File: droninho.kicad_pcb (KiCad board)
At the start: 2 copper layers, 49 x 72.2 mm, 34 parts, among them J6 I2C, J7 TXD0/RXD0, J8 I2C, Q1 Si2300DS, Q2 Si2300DS, Q3 Si2300DS, Q4 Si2300DS, SW1 KMR241G LFS, U1 AMS1117-3.3, U2 MPU9250/6500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

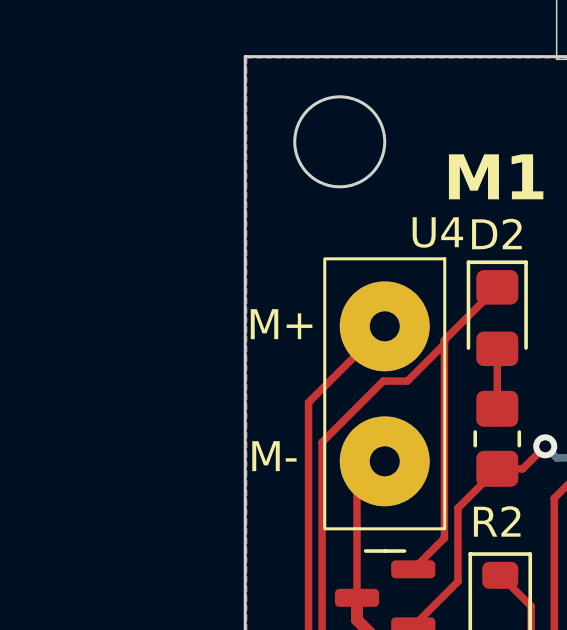
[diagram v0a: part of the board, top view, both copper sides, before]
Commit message: add manufacturer and part number for BOM.
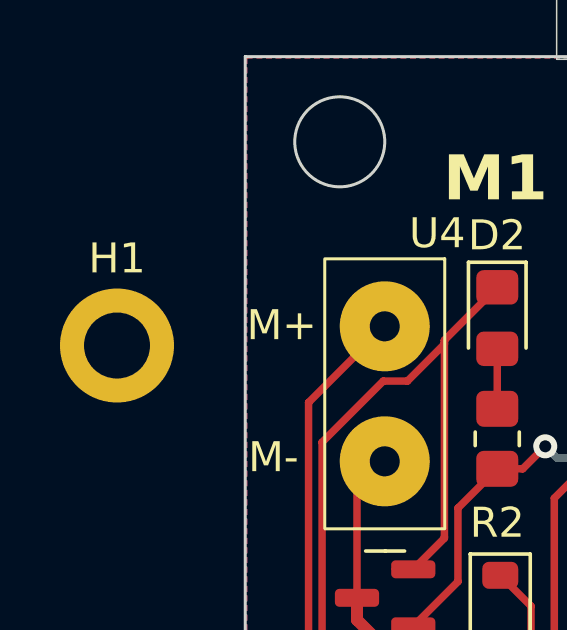
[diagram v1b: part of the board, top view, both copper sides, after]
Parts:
- added H1: MountingHole_Pad_MP, MountingHole:MountingHole_2.2mm_M2_DIN965_Pad, F.Cu at (116.8, 75.7)
- C3: value 0.1uF/50V(10%) -> 0.1uF/10V(5%)
- R1, R2, R3, R4, R5: value 10K(5%) -> 10K(1%)

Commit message: BOM updated.
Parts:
- removed H1: MountingHole_Pad_MP, MountingHole:MountingHole_2.2mm_M2_DIN965_Pad
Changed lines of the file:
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@@
 		)
 	)
-	(footprint "MountingHole:MountingHole_2.2mm_M2_DIN965_Pad"
-		(layer "F.Cu")
-		(at 116.775 75.69)
-		(descr "Mounting Hole 2.2mm, M2, DIN965")
-		(tags "mounting hole 2.2mm m2 din965")
-		(property "Reference" "H1"
-			(at 0 -2.9 0)
-			(layer "F.SilkS")
-			(effects
-				(font
-					(size 1 1)
-					(thickness 0.15)
-				)
-			)
-		)
-		(property "Value" "MountingHole_Pad_MP"
-			(at 0 2.9 0)
-			(layer "F.Fab")
-			(effects
-				(font
-					(size 1 1)
-					(thickness 0.15)
-				)
-			)
-		)
-		(property "Datasheet" ""
-			(at 0 0 0)
-			(unlocked yes)
-			(layer "F.Fab")
-			(hide yes)
-			(effects
-				(font
-					(size 1.27 1.27)
-					(thickness 0.15)
-				)
-			)
-		)
-		(property "Description" "Mounting Hole with connection as pad named MP"
-			(at 0 0 0)
-			(unlocked yes)
-			(layer "F.Fab")
-			(hide yes)
-			(effects
-				(font
-					(size 1.27 1.27)
-					(thickness 0.15)
-				)
-			)
-		)
-		(property "Manufacturer" ""
-			(at 0 0 0)
-			(unlocked yes)
-			(layer "F.Fab")
-			(hide yes)
-			(effects
-				(font
-					(size 1 1)
-					(thickness 0.15)
-				)
-			)
-		)
-		(property "Mfg Part #" ""
-			(at 0 0 0)
-			(unlocked yes)
-			(layer "F.Fab")
-			(hide yes)
-			(effects
-				(font
-					(size 1 1)
-					(thickness 0.15)
-				)
-			)
-		)
-		(property "Package/Footprint" ""
-			(at 0 0 0)
-			(unlocked yes)
-			(layer "F.Fab")
-			(hide yes)
-			(effects
-				(font
-					(size 1 1)
-					(thickness 0.15)
-				)
-			)
-		)
-		(property "Type" ""
-			(at 0 0 0)
-			(unlocked yes)
-			(layer "F.Fab")
-			(hide yes)
-			(effects
-				(font
-					(size 1 1)
-					(thickness 0.15)
-				)
-			)
-		)
-		(property "Designator" ""
-			(at 0 0 0)
-			(unlocked yes)
-			(layer "F.Fab")
-			(hide yes)
-			(effects
-				(font
-					(size 1 1)
-					(thickness 0.15)
-				)
-			)
-		)
-		(property ki_fp_filters "MountingHole*Pad*")
-		(sheetname "/")
-		(sheetfile "droninho.kicad_sch")
-		(attr exclude_from_pos_files exclude_from_bom)
-		(fp_circle
-			(center 0 0)
-			(end 1.9 0)
-			(stroke
-				(width 0.15)
-				(type solid)
-			)
-			(fill no)
-			(layer "Cmts.User")
-		)
-		(fp_circle
-			(center 0 0)
-			(end 2.15 0)
-			(stroke
-				(width 0.05)
-				(type solid)
-			)
-			(fill no)
-			(layer "F.CrtYd")
-		)
-		(fp_text user "${REFERENCE}"
-			(at 0 0 0)
-			(layer "F.Fab")
-			(effects
-				(font
-					(size 1 1)
-					(thickness 0.15)
-				)
-			)
-		)
-		(pad "1" thru_hole circle
-			(at 0 0)
-			(size 3.8 3.8)
-			(drill 2.2)
-			(layers "*.Cu" "*.Mask")
-			(remove_unused_layers no)
-		)
-		(embedded_fonts no)
-	)
 	(footprint "Package_TO_SOT_SMD:SOT-23"
 		(layer "F.Cu")
@@
 			)
 		)
+		(property "Manufacturer" "Molex"
+			(at 0 0 180)
+			(unlocked yes)
+			(layer "F.Fab")
+			(hide yes)
+			(effects
+				(font
+					(size 1 1)
+					(thickness 0.15)
+				)
+			)
+		)
+		(property "Mfg Part #" "502603-0470"
+			(at 0 0 180)
+			(unlocked yes)
+			(layer "F.Fab")
+			(hide yes)
+			(effects
+				(font
+					(size 1 1)
+					(thickness 0.15)
+				)
+			)
+		)
+		(property "Package/Footprint" "4POS"
+			(at 0 0 180)
+			(unlocked yes)
+			(layer "F.Fab")
+			(hide yes)
+			(effects
+				(font
+					(size 1 1)
+					(thickness 0.15)
+				)
+			)
+		)
+		(property "Type" "THT"
+			(at 0 0 180)
+			(unlocked yes)
+			(layer "F.Fab")
+			(hide yes)
+			(effects
+				(font
+					(size 1 1)
+					(thickness 0.15)
+				)
+			)
+		)
+		(property "Designator" "J7"
+			(at 0 0 180)
+			(unlocked yes)
+			(layer "F.Fab")
+			(hide yes)
+			(effects
+				(font
+					(size 1 1)
+					(thickness 0.15)
+				)
+			)
+		)
 		(property ki_fp_filters "Connector*:*_1x??_*")
 		(sheetname "/")
@@
 			)
 		)
+		(property "Manufacturer" "Molex"
+			(at 0 0 180)
+			(unlocked yes)
+			(layer "F.Fab")
+			(hide yes)
+			(effects
+				(font
+					(size 1 1)
+					(thickness 0.15)
+				)
+			)
+		)
+		(property "Mfg Part #" "502603-0470"
+			(at 0 0 180)
+			(unlocked yes)
+			(layer "F.Fab")
+			(hide yes)
+			(effects
+				(font
+					(size 1 1)
+					(thickness 0.15)
+				)
+			)
+		)
+		(property "Package/Footprint" "4POS"
+			(at 0 0 180)
+			(unlocked yes)
+			(layer "F.Fab")
+			(hide yes)
+			(effects
+				(font
+					(size 1 1)
+					(thickness 0.15)
+				)
+			)
+		)
+		(property "Type" "THT"
+			(at 0 0 180)
+			(unlocked yes)
+			(layer "F.Fab")
+			(hide yes)
+			(effects
+				(font
+					(size 1 1)
+					(thickness 0.15)
+				)
+			)
+		)
+		(property "Designator" "J8"
+			(at 0 0 180)
+			(unlocked yes)
+			(layer "F.Fab")
+			(hide yes)
+			(effects
+				(font
+					(size 1 1)
+					(thickness 0.15)
+				)
+			)
+		)
 		(property ki_fp_filters "Connector*:*_1x??_*")
 		(sheetname "/")
@@
 			)
 		)
+		(property "Manufacturer" "C&K"
+			(at 0 0 0)
+			(unlocked yes)
+			(layer "F.Fab")
+			(hide yes)
+			(effects
+				(font
+					(size 1 1)
+					(thickness 0.15)
+				)
+			)
+		)
+		(property "Mfg Part #" "KMR241G LFS"
+			(at 0 0 0)
+			(unlocked yes)
+			(layer "F.Fab")
+			(hide yes)
+			(effects
+				(font
+					(size 1 1)
+					(thickness 0.15)
+				)
+			)
+		)
+		(property "Package/Footprint" "SW_Push_1P1T_NO_CK_KMR2"
+			(at 0 0 0)
+			(unlocked yes)
+			(layer "F.Fab")
+			(hide yes)
+			(effects
+				(font
+					(size 1 1)
+					(thickness 0.15)
+				)
+			)
+		)
+		(property "Type" "SMT"
+			(at 0 0 0)
+			(unlocked yes)
+			(layer "F.Fab")
+			(hide yes)
+			(effects
+				(font
+					(size 1 1)
+					(thickness 0.15)
+				)
+			)
+		)
+		(property "Designator" "SW1"
+			(at 0 0 0)
+			(unlocked yes)
+			(layer "F.Fab")
+			(hide yes)
+			(effects
+				(font
+					(size 1 1)
+					(thickness 0.15)
+				)
+			)
+		)
 		(sheetname "/")
 		(sheetfile "droninho.kicad_sch")
@@
 			(at 0 0 0)
 			(unlocked yes)
+			(layer "F.Fab")
+			(hide yes)
+			(effects
+				(font
+					(size 1 1)
+					(thickness 0.15)
+				)
+			)
+		)
+		(property "Manufacturer" "Molex"
+			(at 0 0 0)
+			(unlocked yes)
+			(layer "F.Fab")
+			(hide yes)
+			(effects
+				(font
+					(size 1 1)
+					(thickness 0.15)
+				)
+			)
+		)
+		(property "Mfg Part #" "502603-0470"
+			(at 0 0 0)
+			(unlocked yes)
+			(layer "F.Fab")
+			(hide yes)
+			(effects
+				(font
+					(size 1 1)
+					(thickness 0.15)
+				)
+			)
+		)
+		(property "Package/Footprint" "4POS"
+			(at 0 0 0)
+			(unlocked yes)
+			(layer "F.Fab")
+			(hide yes)
+			(effects
+				(font
+					(size 1 1)
+					(thickness 0.15)
+				)
+			)
+		)
+		(property "Type" "THT"
+			(at 0 0 0)
+			(unlocked yes)
+			(layer "F.Fab")
+			(hide yes)
+			(effects
+				(font
+					(size 1 1)
+					(thickness 0.15)
+				)
+			)
+		)
+		(property "Designator" "J6"
+			(at 0 0 0)
+			(unlocked yes)

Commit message: first commit
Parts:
- added C4: 0.1uF/10V(5%), Capacitor_SMD:C_0402_1005Metric, F.Cu at (146.0, 125.2)
- added C5: 0.1uF/10V(5%), Capacitor_SMD:C_0402_1005Metric, F.Cu at (148.9, 121.1)
- added C6: 0.1uF/10V(5%), Capacitor_SMD:C_0402_1005Metric, F.Cu at (155.9, 126.2)
- added C7: 0.1uF/10V(5%), Capacitor_SMD:C_0402_1005Metric, F.Cu at (155.9, 128.2)
- added C8: C_Small_US, Capacitor_SMD:C_0201_0603Metric, F.Cu at (155.7, 130.0)
- added U8: ICM-20948, Sensor_Motion:InvenSense_QFN-24_3x3mm_P0.4mm, F.Cu at (144.9, 121.6)
- U2: value MPU9250/6500 -> TLV70218_SOT23-5; footprint Library:MPU-9250-6500 -> Package_TO_SOT_SMD:SOT-23-5
- moved U2 19.6 mm to (151.9, 127.6), turned to 0 degrees
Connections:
- U2 pad 1: /+3.3V -> Net-(U2-EN)
- U2 pad 3: /SCL -> Net-(U2-EN)
- U2 pad 4: /SDA -> unconnected-(U2-NC-Pad4)
- U2 pad 5: unconnected-(U2-EDA-Pad5) -> Net-(U2-OUT)
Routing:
- net GND: track 228.1 -> 0.00 mm, vias 3 -> 0
- net /+3.3V: track 199.1 -> 0.00 mm, vias 5 -> 0
- net /PWM3: track 80.6 -> 0.00 mm, vias 2 -> 0
- net /PWM4: track 77.0 -> 0.00 mm, vias 3 -> 0
- net /SCL: track 72.0 -> 0.00 mm, vias 1 -> 0
- net /SDA: track 65.9 -> 0.00 mm, vias 1 -> 0
- net /PWM2: track 59.4 -> 0.00 mm, vias 2 -> 0
- net /TXD0: track 54.0 -> 0.00 mm, vias 1 -> 0
- net /TXD2: track 48.5 -> 0.00 mm, vias 2 -> 0
- net /BAT+: track 48.3 -> 0.00 mm, vias 4 -> 0
- net /RXD0: track 47.6 -> 0.00 mm, vias 1 -> 0
- net /RXD2: track 42.2 -> 0.00 mm, vias 2 -> 0
- net /PWM1: track 36.4 -> 0.00 mm, vias 1 -> 0
- net /Push_button: track 31.8 -> 0.00 mm
- net /M4-: track 11.4 -> 0.00 mm, vias 1 -> 0
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- removed copper zone on B.Cu, net GND
- removed copper zone on F.Cu, net GND
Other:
- outline, holes or cut-outs redrawn
- board text removed: "MPU925/6500"

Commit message: driver PCB ready
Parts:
- removed C3: 0.1uF/10V(5%), Capacitor_SMD:C_0805_2012Metric_Pad1.18x1.45mm_HandSolder
- removed C4, C5, C6, C7: 0.1uF/10V(5%), Capacitor_SMD:C_0402_1005Metric
- removed C8: C_Small_US, Capacitor_SMD:C_0201_0603Metric
- removed J6, J8: I2C, Connector_PinHeader_2.54mm:PinHeader_1x04_P2.54mm_Vertical
- removed J7: TXD0/RXD0, Connector_PinHeader_2.54mm:PinHeader_1x04_P2.54mm_Vertical
- removed SW1: KMR241G LFS, Button_Switch_SMD:SW_Push_1P1T_NO_CK_KMR2
- removed U2: TLV70218_SOT23-5, Package_TO_SOT_SMD:SOT-23-5
- removed U3: ESP32 ESP-WROOM-32 DEVKit V1, Library:ESP32_30pin vertical WIFI
- removed U4, U5, U6, U7: Through Hole Connector, Library:Connector_Motor
- removed U8: ICM-20948, Sensor_Motion:InvenSense_QFN-24_3x3mm_P0.4mm
- added J1: Conn_01x06_Socket, Connector_Hirose:Hirose_DF13-06P-1.25DSA_1x06_P1.25mm_Vertical, F.Cu at (61.9, 57.5)
- added J2: Conn_01x02_Socket, Connector_Hirose:Hirose_DF13-02P-1.25DSA_1x02_P1.25mm_Vertical, F.Cu at (54.6, 58.5)
- added J3: Conn_01x02_Socket, Connector_Hirose:Hirose_DF13-02P-1.25DSA_1x02_P1.25mm_Vertical, F.Cu at (75.6, 57.4)
- added J4: Conn_01x02_Socket, Connector_Hirose:Hirose_DF13-02P-1.25DSA_1x02_P1.25mm_Vertical, F.Cu at (75.7, 71.8)
- added J5: Conn_01x02_Socket, Connector_Hirose:Hirose_DF13-02P-1.25DSA_1x02_P1.25mm_Vertical, F.Cu at (54.4, 72.9)
- moved R3 112.9 mm to (70.3, 61.5)
- moved D3 108.6 mm to (72.6, 61.5), turned to 90 degrees
- moved R5 103.3 mm to (58.2, 69.2), turned to 180 degrees
- moved Q3 101.9 mm to (76.5, 67.9)
- moved D5 100.6 mm to (60.6, 71.3), turned to 180 degrees
- moved H4 100.4 mm to (68.1, 75.0)
- moved H3 100.4 mm to (62.3, 75.0)
- moved D8 98.9 mm to (72.8, 73.7)
- moved D7 93.2 mm to (72.5, 57.0)
- moved C1 92.2 mm to (59.3, 66.5)
- moved Q2 91.7 mm to (76.5, 62.6)
- moved Q4 90.0 mm to (53.3, 67.8)
- moved D9 85.8 mm to (57.4, 74.0)
- moved R4 83.8 mm to (72.0, 69.2), turned to 180 degrees
- moved D4 81.1 mm to (69.7, 71.4), turned to 0 degrees
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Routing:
- net GND: track 0.00 -> 86.0 mm, vias 0 -> 7
- net /+3.3V: track 0.00 -> 76.0 mm, vias 0 -> 5
- net /BAT+: track 0.00 -> 25.3 mm, vias 0 -> 2
- net /PWM4: track 0.00 -> 23.9 mm, vias 0 -> 1
- net /PWM3: track 0.00 -> 20.6 mm, vias 0 -> 2
- net /PWM2: track 0.00 -> 18.9 mm, vias 0 -> 2
- net /PWM1: track 0.00 -> 13.5 mm
- net /M4-: track 0.00 -> 10.3 mm
- net /M2-: track 0.00 -> 10.3 mm
- net /M1-: track 0.00 -> 8.16 mm
- net /M3-: track 0.00 -> 7.57 mm
- net Net-(D5-A): track 0.00 -> 3.26 mm
- net Net-(D4-A): track 0.00 -> 2.34 mm
- net Net-(D3-A): track 0.00 -> 2.32 mm
- net Net-(D2-A): track 0.00 -> 2.21 mm
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- added copper zone on B.Cu, net GND
- added copper zone on F.Cu, net GND
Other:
- board size 49 x 72.2 mm -> 30 x 30 mm
- board text added: "+ -"
- board text added: "+3.3v"
- board text added: "- +"
- board text added: "12v max"
- board text added: "B+"
- board text added: "B-"
- board text added: "PWM1"
- board text added: "PWM2"
- board text added: "PWM3"
- board text added: "PWM4"
- board text added: "UFABC"
- board text added: "V1.1"
- board text added: "github.com/dferruzzo/Droninho/tree/driver"
- board text removed: "3.3v"
- board text removed: "BAT+"
- board text removed: "BAT-"
- board text removed: "Droninho Taphros 2025 v1.0"
- board text removed: "ESP32-DevKit"
- board text removed: "RX0"
- board text removed: "RX2"
- board text removed: "SCL"
- board text removed: "SDA"
- board text removed: "TX0"
- board text removed: "TX2"
- board text removed: "https://github.com/dferruzzo/Droninho"

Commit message: small updates
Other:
- board text added: "M1+ M1-"
- board text added: "M2- M2+"
- board text added: "M3- M3+"
- board text added: "M4+ M4-"
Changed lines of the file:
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@@
+		)
+	)
+	(gr_text "12v\nmax"
+		(at 65 79.5 0)
+		(layer "F.SilkS")
+		(effects
+			(font
+				(size 1 1)
+				(thickness 0.15)
+			)
+			(justify bottom)
 		)
 	)
 	(gr_text "PWM4"
-		(at 68.8 54.8 90)
+		(at 68.85 54.8 90)
 		(layer "F.SilkS")
 		(effects
@@
 	)
 	(gr_text "+3.3v"
-		(at 62.3 54.8 90)
+		(at 62.25 54.8 90)
 		(layer "F.SilkS")
 		(effects
@@
 		)
 	)
-	(gr_text "12v\nmax"
-		(at 63.6 79.7 0)
-		(layer "F.SilkS")
-		(effects
-			(font
-				(size 1 1)
-				(thickness 0.15)
-			)
-			(justify left bottom)
-		)
-	)
 	(gr_text "+\n-"
 		(at 50.1 73.9 0)
@@
 		)
 	)
+	(gr_text "PWM1"
+		(at 64.9 53.3 90)
+		(layer "B.SilkS")
+		(effects
+			(font
+				(size 0.8 0.75)
+				(thickness 0.15)
+			)
+			(justify left bottom mirror)
+		)
+	)
+	(gr_text "M3-\nM3+"
+		(at 79.8 73.85 0)
+		(layer "B.SilkS")
+		(effects
+			(font
+				(size 1 1)
+				(thickness 0.15)
+			)
+			(justify left bottom mirror)
+		)
+	)
+	(gr_text "PWM3"
+		(at 67.5 53.3 90)
+		(layer "B.SilkS")
+		(effects
+			(font
+				(size 0.8 0.75)
+				(thickness 0.15)
+			)
+			(justify left bottom mirror)
+		)
+	)
+	(gr_text "PWM4"
+		(at 68.8 53.3 90)
+		(layer "B.SilkS")
+		(effects
+			(font
+				(size 0.8 0.75)
+				(thickness 0.15)
+			)
+			(justify left bottom mirror)
+		)
+	)
+	(gr_text "M2-\nM2+"
+		(at 79.7 59.45 0)
+		(layer "B.SilkS")
+		(effects
+			(font
+				(size 1 1)
+				(thickness 0.15)
+			)
+			(justify left bottom mirror)
+		)
+	)
+	(gr_text "+3.3v"
+		(at 62.3 53.1 90)
+		(layer "B.SilkS")
+		(effects
+			(font
+				(size 0.8 0.75)
+				(thickness 0.15)
+			)
+			(justify left bottom mirror)
+		)
+	)
 	(gr_text "B+\n"
 		(at 63.6 79 0)
@@
 		)
 	)
+	(gr_text "GND"
+		(at 63.6 53.3 90)
+		(layer "B.SilkS")
+		(effects
+			(font
+				(size 0.8 0.75)
+				(thickness 0.15)
+			)
+			(justify left bottom mirror)
+		)
+	)
+	(gr_text "M4+\nM4-"
+		(at 53.75 73.85 0)
+		(layer "B.SilkS")
+		(effects
+			(font
+				(size 1 1)
+				(thickness 0.15)
+			)
+			(justify left bottom mirror)
+		)
+	)
 	(gr_text "github.com/dferruzzo/Droninho/tree/driver"
 		(at 78.3 69.6 0)
@@
 				(thickness 0.15)
 			)
+			(justify left bottom mirror)
+		)
+	)
+	(gr_text "M1+\nM1-"
+		(at 53.9 59.45 0)
+		(layer "B.SilkS")
+		(effects
+			(font
+				(size 1 1)
+				(thickness 0.15)
+			)
+			(justify left bottom mirror)
+		)
+	)
+	(gr_text "PWM2"
+		(at 66.2 53.3 90)
+		(layer "B.SilkS")
+		(effects
+			(font
+				(size 0.8 0.75)
+				(thickness 0.15)
+			)

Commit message: driver finalizado.
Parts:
- J1: footprint Connector_Hirose:Hirose_DF13-06P-1.25DSA_1x06_P1.25mm_Vertical -> Connector_JST:JST_PH_B6B-PH-K_1x06_P2.00mm_Vertical
- J2, J3, J4, J5: footprint Connector_Hirose:Hirose_DF13-02P-1.25DSA_1x02_P1.25mm_Vertical -> Connector_JST:JST_PH_B2B-PH-K_1x02_P2.00mm_Vertical
- moved J1 3.62 mm to (60.0, 54.4)
- moved D7 2.36 mm to (71.1, 59.0), turned to 0 degrees
- moved J3 2.24 mm to (76.9, 55.6)
- moved D6 2.09 mm to (58.9, 58.9), turned to 180 degrees
- moved J5 1.99 mm to (53.1, 74.4)
- moved D5 1.83 mm to (62.4, 71.0)
- moved J2 1.78 mm to (53.1, 57.5)
- moved J4 1.48 mm to (77.0, 72.5)
- moved D8 1.32 mm to (71.7, 74.4)
- moved D9 1.28 mm to (58.6, 73.5)
- moved D3 1.02 mm to (71.8, 62.0)
- moved R3 0.81 mm to (69.7, 62.0)
- moved D4 0.63 mm to (70.2, 71.0)
- moved D2 0.54 mm to (58.1, 62.0)
- moved R2 0.52 mm to (60.3, 62.0)
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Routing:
- net /+3.3V: track 76.0 -> 111.2 mm, vias 5 -> 4
- net /PWM4: track 23.9 -> 32.2 mm
- net GND: track 86.0 -> 81.2 mm, vias 7 -> 6
- net /PWM1: track 13.5 -> 17.0 mm
- net /M4-: track 10.3 -> 13.6 mm
- net /M3-: track 7.57 -> 10.5 mm
- net /PWM2: track 18.9 -> 16.5 mm, vias 2 -> 0
- net Net-(D5-A): track 3.26 -> 5.27 mm
- net /M1-: track 8.16 -> 9.64 mm
- net /M2-: track 10.3 -> 11.0 mm
- net /BAT+: track 25.3 -> 25.5 mm, vias 2 -> 4
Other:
- outline, holes or cut-outs redrawn
- board text removed: "+ -"
- board text removed: "- +"
- board text removed: "M1"
- board text removed: "M2"
- board text removed: "M3"
- board text removed: "M4"
